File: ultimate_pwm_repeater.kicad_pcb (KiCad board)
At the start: 2 copper layers, 48.5 x 40.5 mm, 21 parts, among them J1 POWER, J2 SIGNAL, Q1 IRF3205, Q2 IRF3205, Q3 IRF3205, Q4 IRF3205

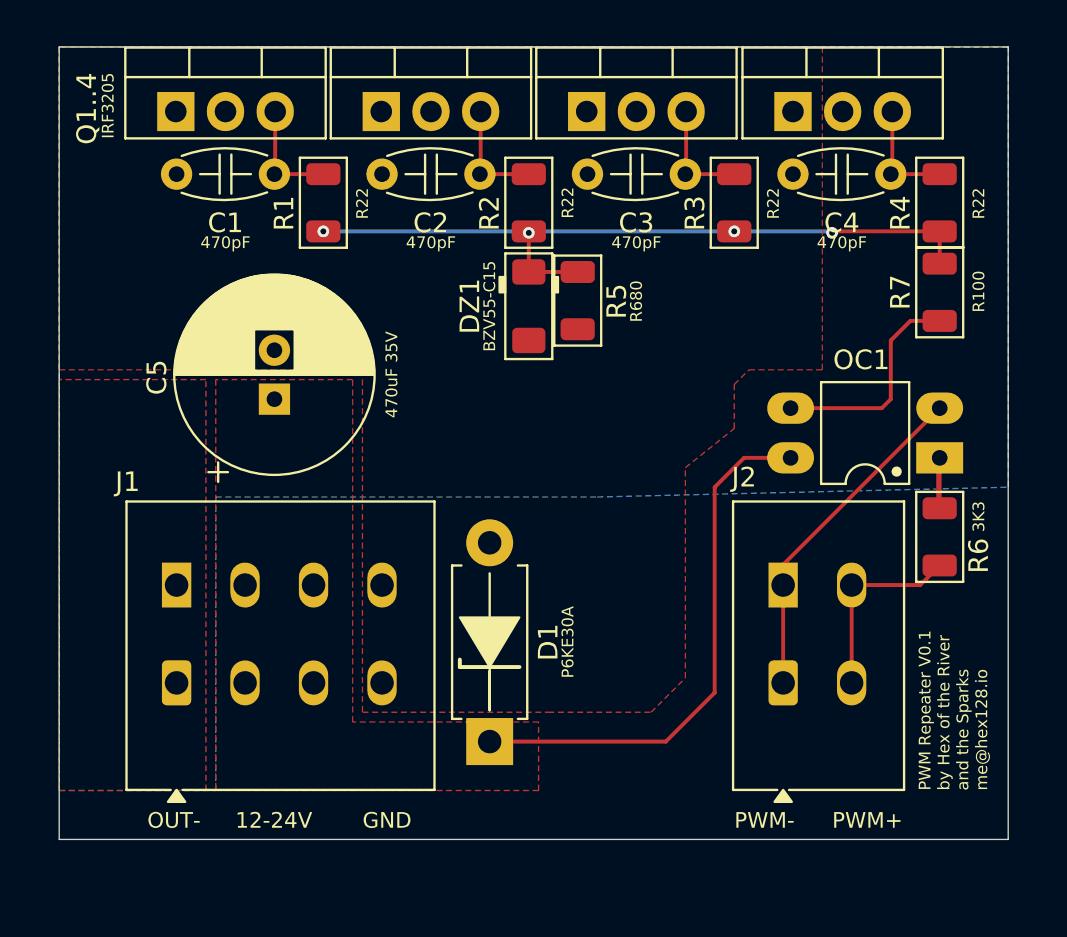
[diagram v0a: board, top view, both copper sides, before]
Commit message: replaced connectors
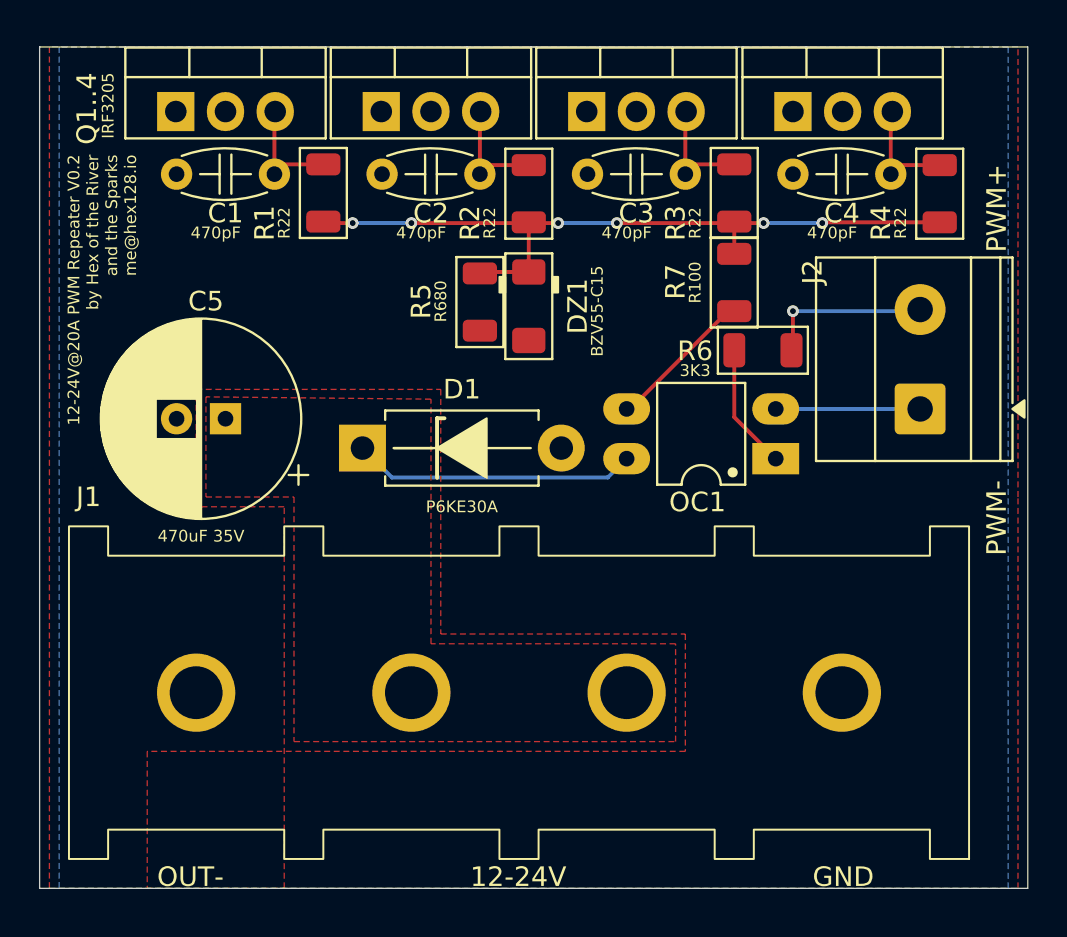
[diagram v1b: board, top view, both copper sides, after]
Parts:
- J1: footprint TerminalBlock_WAGO:TerminalBlock_WAGO_2601-1104_1x04_P3.50mm_Horizontal -> TerminalBlock:TerminalBlock_Degson_DG65C-B-04P
- J2: footprint TerminalBlock_WAGO:TerminalBlock_WAGO_2601-1102_1x02_P3.50mm_Horizontal -> TerminalBlock_Phoenix:TerminalBlock_Phoenix_MKDS-1,5-2-5.08_1x02_P5.08mm_Horizontal
- moved J1 17.5 mm to (63.0, 72.0)
- moved D1 16.3 mm to (55.0, 59.5), turned to 0 degrees
- moved J2 15.7 mm to (83.5, 57.5), turned to 90 degrees
- moved R6 13.1 mm to (75.5, 54.5), turned to 0 degrees
- moved R7 10.5 mm to (74.0, 51.0)
- moved OC1 8.38 mm to (76.1, 60.0)
- moved R5 5.00 mm to (61.0, 52.0)
- moved C5 2.69 mm to (48.0, 58.0), turned to 180 degrees
- moved R1 0.50 mm to (53.0, 46.5)
- moved R3 0.50 mm to (74.0, 46.5)
- moved R2 0.46 mm to (63.5, 46.5)
- moved R4 0.46 mm to (84.5, 46.5)
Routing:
- net +24V: track 27.5 -> 14.5 mm
- net PWM-: track 17.4 -> 6.88 mm
- net Net-(OC1-Pad3): track 11.3 -> 7.70 mm
- net PWM+: track 9.91 -> 8.03 mm, vias 0 -> 1
- net Net-(OC1-Pad1): track 5.61 -> 6.42 mm
- net Net-(DZ1-K): track 37.8 -> 38.4 mm, vias 4 -> 6
- removed copper zone on F.Cu, net OUT-
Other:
- board size 48.5 x 40.5 mm -> 50.5 x 43 mm
- board text added: "12-24V@20A PWM Repeater V0.2 by Hex of the River and the Sparks me@hex128.io"
- board text removed: "PWM Repeater V0.1 by Hex of the River and the Sparks me@hex128.io"
